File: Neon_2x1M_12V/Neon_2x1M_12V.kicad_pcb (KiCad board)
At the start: 2 copper layers, 77.5 x 51.5 mm, 47 parts, among them J2 Barrel_Jack_MountingPin, J4 Barrel_Jack_MountingPin, J5 Barrel_Jack_MountingPin, J6 Conn_01x03_Pin, Q1 IRLML2502TRPBF, Q2 IRLML2502TRPBF, Q3 BSS138, Q4 BSS138, Q5 BSS138, SW1 SW_Push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

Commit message: added vias to 12v routes
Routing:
- net +12V: vias 6 -> 7
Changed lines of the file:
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@@
-	)
-	(segment
-		(start 171.9 52.1)
-		(end 171.9 55.8)
-		(width 1.27)
-		(layer "F.Cu")
-		(net 1)
 	)
 	(segment
@@
 	)
 	(segment
-		(start 183.3 59.9)
-		(end 183.3 67.5)
-		(width 1.27)
-		(layer "F.Cu")
-		(net 1)
-	)
-	(segment
-		(start 171.9 55.8)
-		(end 171.9 63.9575)
+		(start 171.9 55.8)
+		(end 179.2 55.8)
 		(width 1.27)
 		(layer "F.Cu")
@@
 	)
 	(segment
-		(start 171.9 55.8)
-		(end 179.2 55.8)
-		(width 1.27)
-		(layer "F.Cu")
-		(net 1)
-	)
-	(segment
 		(start 171.9 63.9575)
 		(end 172.7 64.7575)
@@
 	)
 	(segment
+		(start 171.9 52.1)
+		(end 172.7 51.3)
+		(width 1.27)
+		(layer "F.Cu")
+		(net 1)
+	)
+	(segment
+		(start 179.2 55.8)
+		(end 183.3 59.9)
+		(width 1.27)
+		(layer "F.Cu")
+		(net 1)
+	)
+	(segment
+		(start 171.9 55.8)
+		(end 171.9 52.1)
+		(width 1.27)
+		(layer "F.Cu")
+		(net 1)
+	)
+	(segment
 		(start 118.367677 61)
 		(end 118.4 61)
@@
 	)
 	(segment
-		(start 172.7 51.3)
-		(end 171.9 52.1)
-		(width 1.27)
-		(layer "F.Cu")
-		(net 1)
-	)
-	(segment
 		(start 124.2 52)
 		(end 124.2 55.825)
@@
 	)
 	(segment
+		(start 118.367677 62.867677)
+		(end 118.367677 61)
+		(width 1.27)
+		(layer "F.Cu")
+		(net 1)
+	)
+	(segment
+		(start 171.9 55.8)
+		(end 171.9 63.9575)
+		(width 1.27)
+		(layer "F.Cu")
+		(net 1)
+	)
+	(segment
+		(start 183.3 59.9)
+		(end 183.3 67.5)
+		(width 1.27)
+		(layer "F.Cu")
+		(net 1)
+	)
+	(segment
+		(start 122.8 67.3)
+		(end 123.7 67.3)
+		(width 1.27)
+		(layer "F.Cu")
+		(net 1)
+	)
+	(segment
+		(start 159 72.6)
+		(end 170.8 72.6)
+		(width 1.27)
+		(layer "F.Cu")
+		(net 1)
+	)
+	(segment
+		(start 123.342676 56.025)
+		(end 121.683838 57.683838)
+		(width 1.27)
+		(layer "F.Cu")
+		(net 1)
+	)
+	(segment
+		(start 124 56.025)
+		(end 123.342676 56.025)
+		(width 1.27)
+		(layer "F.Cu")
+		(net 1)
+	)
+	(segment
 		(start 183.3 67.5)
 		(end 178.2 72.6)
-		(width 1.27)
-		(layer "F.Cu")
-		(net 1)
-	)
-	(segment
-		(start 118.367677 62.867677)
-		(end 118.367677 61)
-		(width 1.27)
-		(layer "F.Cu")
-		(net 1)
-	)
-	(segment
-		(start 179.2 55.8)
-		(end 183.3 59.9)
-		(width 1.27)
-		(layer "F.Cu")
-		(net 1)
-	)
-	(segment
-		(start 122.8 67.3)
-		(end 123.7 67.3)
-		(width 1.27)
-		(layer "F.Cu")
-		(net 1)
-	)
-	(segment
-		(start 159 72.6)
-		(end 170.8 72.6)
-		(width 1.27)
-		(layer "F.Cu")
-		(net 1)
-	)
-	(segment
-		(start 123.342676 56.025)
-		(end 121.683838 57.683838)
-		(width 1.27)
-		(layer "F.Cu")
-		(net 1)
-	)
-	(segment
-		(start 124 56.025)
-		(end 123.342676 56.025)
 		(width 1.27)
 		(layer "F.Cu")
@@
 	)
 	(via
+		(at 171.9 55.8)
+		(size 1.5)
+		(drill 0.75)
+		(layers "F.Cu" "B.Cu")
+		(net 1)
+	)
+	(via
 		(at 159 72.6)
 		(size 1.5)
@@
 		(drill 0.75)
 		(layers "F.Cu" "B.Cu")
+		(net 1)
+	)
+	(segment
+		(start 121.683838 57.683838)
+		(end 121.667676 57.7)
+		(width 1.27)
+		(layer "B.Cu")
+		(net 1)
+	)
+	(segment
+		(start 118.367677 59.032323)
+		(end 119.716162 57.683838)
+		(width 1.27)
+		(layer "B.Cu")
+		(net 1)
+	)
+	(segment
+		(start 124.2 52)
+		(end 122.7 50.5)
+		(width 1.27)
+		(layer "B.Cu")
+		(net 1)
+	)
+	(segment
+		(start 122.7 50.5)
+		(end 122.7 49.2)
+		(width 1.27)
+		(layer "B.Cu")
+		(net 1)
+	)
+	(segment
+		(start 171.9 52.1)
+		(end 172.7 51.3)
+		(width 1.27)
+		(layer "B.Cu")
+		(net 1)
+	)
+	(segment
+		(start 121.683838 57.683838)
+		(end 124.2 55.167677)
+		(width 1.27)
+		(layer "B.Cu")
+		(net 1)
+	)
+	(segment
+		(start 118.367677 62.867677)
+		(end 118.367677 61)
+		(width 1.27)
+		(layer "B.Cu")
+		(net 1)
+	)
+	(segment
+		(start 170.8 72.6)
+		(end 172.7 70.7)
+		(width 1.27)
+		(layer "B.Cu")
+		(net 1)
+	)
+	(segment
+		(start 171.9 55.8)
+		(end 171.9 63.9575)
+		(width 1.27)
+		(layer "B.Cu")
+		(net 1)
+	)
+	(segment
+		(start 119.99 64.49)
+		(end 120.09 64.49)
+		(width 1.27)
+		(layer "B.Cu")
+		(net 1)
+	)
+	(segment
+		(start 119.99 64.49)
+		(end 118.367677 62.867677)
+		(width 1.27)
+		(layer "B.Cu")
+		(net 1)
+	)
+	(segment
+		(start 119.716162 57.683838)
+		(end 121.683838 57.683838)
+		(width 1.27)
+		(layer "B.Cu")
+		(net 1)
+	)
+	(segment
+		(start 124.2 55.167677)
+		(end 124.2 53.3)
+		(width 1.27)
+		(layer "B.Cu")
+		(net 1)
+	)
+	(segment
+		(start 172.7 70.7)
+		(end 172.7 64.7575)
+		(width 1.27)
+		(layer "B.Cu")
+		(net 1)
+	)
+	(segment
+		(start 124.2 53.3)
+		(end 124.2 52)
+		(width 1.27)
+		(layer "B.Cu")
 		(net 1)
 	)
@@
 	)
 	(segment
-		(start 121.683838 57.683838)
-		(end 121.667676 57.7)
-		(width 1.27)
-		(layer "B.Cu")
-		(net 1)
-	)
-	(segment
-		(start 118.367677 59.032323)
-		(end 119.716162 57.683838)
-		(width 1.27)
-		(layer "B.Cu")
-		(net 1)
-	)
-	(segment
-		(start 124.2 52)
-		(end 122.7 50.5)
-		(width 1.27)
-		(layer "B.Cu")
-		(net 1)
-	)
-	(segment
-		(start 122.7 50.5)
-		(end 122.7 49.2)
-		(width 1.27)
-		(layer "B.Cu")
-		(net 1)
-	)
-	(segment
-		(start 121.683838 57.683838)
-		(end 124.2 55.167677)
-		(width 1.27)
-		(layer "B.Cu")
-		(net 1)
-	)
-	(segment
-		(start 118.367677 62.867677)
-		(end 118.367677 61)
-		(width 1.27)
-		(layer "B.Cu")
-		(net 1)
-	)
-	(segment
-		(start 170.8 72.6)
-		(end 172.7 70.7)
-		(width 1.27)
-		(layer "B.Cu")
-		(net 1)
-	)
-	(segment
-		(start 119.99 64.49)
-		(end 120.09 64.49)
-		(width 1.27)
-		(layer "B.Cu")
-		(net 1)
-	)
-	(segment
-		(start 119.99 64.49)
-		(end 118.367677 62.867677)
-		(width 1.27)
-		(layer "B.Cu")
-		(net 1)
-	)
-	(segment
-		(start 119.716162 57.683838)
-		(end 121.683838 57.683838)
-		(width 1.27)
-		(layer "B.Cu")
-		(net 1)
-	)
-	(segment
-		(start 124.2 55.167677)
-		(end 124.2 53.3)
-		(width 1.27)
-		(layer "B.Cu")
-		(net 1)
-	)
-	(segment
-		(start 172.7 70.7)
-		(end 172.7 64.7575)
-		(width 1.27)
-		(layer "B.Cu")
-		(net 1)
-	)
-	(segment
-		(start 124.2 53.3)
-		(end 124.2 52)
-		(width 1.27)
-		(layer "B.Cu")
-		(net 1)
-	)
-	(segment
 		(start 128.2 72.6)
 		(end 170.8 72.6)
@@
 	)
 	(segment
-		(start 171.9 52.1)
-		(end 172.7 51.3)
-		(width 1.27)
-		(layer "B.Cu")
-		(net 1)
-	)
-	(segment
 		(start 120.09 64.49)
 		(end 128.2 72.6)
@@
 	)
 	(segment
+		(start 171.9 55.8)
+		(end 171.9 52.1)
+		(width 1.27)
+		(layer "B.Cu")
+		(net 1)
+	)
+	(segment
 		(start 118.367677 61)
 		(end 118.367677 59.032323)
 		(width 1.27)
 		(layer "B.Cu")
-		(net 1)
-	)
-	(segment
-		(start 171.9 63.9575)
-		(end 171.9 52.1)
-		(width 1.27)
-		(layer "B.Cu")

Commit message: generated BOM
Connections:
- J2 pad 3: (no net) -> unconnected-(J2-MountPin-Pad3)
- J4 pad 3: (no net) -> unconnected-(J4-MountPin-Pad3)
- J5 pad 3: (no net) -> unconnected-(J5-MountPin-Pad3)
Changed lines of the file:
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@@
 	(net 54 "unconnected-(U1-SDI{slash}SD1-Pad22)")
 	(net 55 "unconnected-(U1-SCK{slash}CLK-Pad20)")
+	(net 56 "unconnected-(J2-MountPin-Pad3)")
+	(net 57 "unconnected-(J4-MountPin-Pad3)")
+	(net 58 "unconnected-(J5-MountPin-Pad3)")
 	(footprint "Resistor_SMD:R_0805_2012Metric_Pad1.20x1.40mm_HandSolder"
 		(layer "F.Cu")
@@
 			(remove_unused_layers no)
 			(roundrect_rratio 0.25)
+			(net 57 "unconnected-(J4-MountPin-Pad3)")
+			(pinfunction "MountPin")
+			(pintype "passive+no_connect")
 		)
 		(embedded_fonts no)
@@
 			(remove_unused_layers no)
 			(roundrect_rratio 0.25)
+			(net 58 "unconnected-(J5-MountPin-Pad3)")
+			(pinfunction "MountPin")
+			(pintype "passive+no_connect")
 		)
 		(embedded_fonts no)
@@
 			(remove_unused_layers no)
 			(roundrect_rratio 0.25)
+			(net 56 "unconnected-(J2-MountPin-Pad3)")
+			(pinfunction "MountPin")
+			(pintype "passive+no_connect")
 		)
 		(embedded_fonts no)

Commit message: generated production files
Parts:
- D5: value Blue LED -> Red Indicator LED
- Q3, Q4, Q5: value BSS138 -> Si2302DS
- R1: value 2.2k Ohm -> 820 Ohm
- R13: value 660 Ohm -> 680 Ohm
- R4: value 1k Ohm -> 820 Ohm
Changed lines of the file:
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@@
 			(outputformat 1)
 			(mirror no)
-			(drillshape 1)
+			(drillshape 0)
 			(scaleselection 1)
-			(outputdirectory "")
+			(outputdirectory "Production_Files/Gerbers/")
 		)
 	)
@@
 			)
 		)
-		(property "Value" "BSS138"
+		(property "Value" "Si2302DS"
 			(at 0 2.4 90)
 			(layer "F.Fab")
@@
 			)
 		)
-		(property "Datasheet" "https://www.onsemi.com/pub/Collateral/BSS138-D.PDF"
+		(property "Datasheet" "https://www.vishay.com/docs/68645/si2302cds.pdf"
 			(at 0 0 90)
 			(layer "F.Fab")
@@
 			)
 		)
-		(property "Description" "50V Vds, 0.22A Id, N-Channel MOSFET, SOT-23"
+		(property "Description" ""
 			(at 0 0 90)
 			(layer "F.Fab")
@@
 			)
 		)
-		(property "link" "https://makerselectronics.com/product/smd-mosfet-transistor-bss138-j1-50v-220ma-3-5%CF%8910v220ma-360mw-n-channel-sot-23/?srsltid=AfmBOorKPkIxsAwv-3Onwyym6kfiJ7AE8Pv9g0Pld8GAUTAgILHxbmr_"
+		(property "link" "https://uge-one.com/product/si2302ds-sot23-general-purpose-n-channel-mosfet-smd-transistor-sot-23/"
 			(at 0 0 90)
 			(unlocked yes)
@@
 			)
 		)
-		(property "Value" "2.2k Ohm"
+		(property "Value" "820 Ohm"
 			(at 0 1.83 90)
 			(layer "F.Fab")
@@
 			)
 		)
-		(property "Datasheet" "https://makerselectronics.com/product/chip-resistor-smd-2-2k%cf%89-%c2%b15-0-125w-%c2%b1100ppm-c-0805/"
+		(property "Datasheet" "https://uge-one.com/product/smd-chip-resistor-size-1206-820r-ohm/"
 			(at 0 0 90)
 			(layer "F.Fab")
@@
 			)
 		)
-		(property "link" "https://makerselectronics.com/product/chip-resistor-smd-2-2k%cf%89-%c2%b15-250mw-1206/"
+		(property "link" "https://uge-one.com/product/smd-chip-resistor-size-1206-820r-ohm/"
 			(at 0 0 270)
 			(unlocked yes)
@@
 			)
 		)
-		(property "Value" "Blue LED"
+		(property "Value" "Red Indicator LED"
 			(at 0 1.83 90)
 			(layer "F.Fab")
@@
 			)
 		)
-		(property "Value" "BSS138"
+		(property "Value" "Si2302DS"
 			(at 0.762922 2.733803 0)
 			(layer "F.Fab")
@@
 			)
 		)
-		(property "Datasheet" "https://www.onsemi.com/pub/Collateral/BSS138-D.PDF"
+		(property "Datasheet" "https://www.vishay.com/docs/68645/si2302cds.pdf"
 			(at 0 0 0)
 			(layer "F.Fab")
@@
 			)
 		)
-		(property "Description" "50V Vds, 0.22A Id, N-Channel MOSFET, SOT-23"
+		(property "Description" ""
 			(at 0 0 0)
 			(layer "F.Fab")
@@
 			)
 		)
-		(property "link" "https://makerselectronics.com/product/smd-mosfet-transistor-bss138-j1-50v-220ma-3-5%CF%8910v220ma-360mw-n-channel-sot-23/?srsltid=AfmBOorKPkIxsAwv-3Onwyym6kfiJ7AE8Pv9g0Pld8GAUTAgILHxbmr_"
+		(property "link" "https://uge-one.com/product/si2302ds-sot23-general-purpose-n-channel-mosfet-smd-transistor-sot-23/"
 			(at 0 0 0)
 			(unlocked yes)
@@
 			)
 		)
-		(property "Value" "BSS138"
+		(property "Value" "Si2302DS"
 			(at 0 2.4 90)
 			(layer "F.Fab")
@@
 			)
 		)
-		(property "Datasheet" "https://www.onsemi.com/pub/Collateral/BSS138-D.PDF"
+		(property "Datasheet" "https://www.vishay.com/docs/68645/si2302cds.pdf"
 			(at 0 0 90)
 			(layer "F.Fab")
@@
 			)
 		)
-		(property "Description" "50V Vds, 0.22A Id, N-Channel MOSFET, SOT-23"
+		(property "Description" ""
 			(at 0 0 90)
 			(layer "F.Fab")
@@
 			)
 		)
-		(property "link" "https://makerselectronics.com/product/smd-mosfet-transistor-bss138-j1-50v-220ma-3-5%CF%8910v220ma-360mw-n-channel-sot-23/?srsltid=AfmBOorKPkIxsAwv-3Onwyym6kfiJ7AE8Pv9g0Pld8GAUTAgILHxbmr_"
+		(property "link" "https://uge-one.com/product/si2302ds-sot23-general-purpose-n-channel-mosfet-smd-transistor-sot-23/"
 			(at 0 0 90)
 			(unlocked yes)
@@
 			)
 		)
-		(property "Value" "1k Ohm"
+		(property "Value" "820 Ohm"
 			(at 0 1.83 90)
 			(layer "F.Fab")
@@
 			)
 		)
-		(property "Datasheet" "https://makerselectronics.com/product/chip-resistor-smd-1k%cf%89-%c2%b15-0-125w-%c2%b1100ppm-%e2%84%83-0603/"
+		(property "Datasheet" "https://uge-one.com/product/smd-chip-resistor-size-1206-820r-ohm/"
 			(at 0 0 90)
 			(layer "F.Fab")
@@
 			)
 		)
-		(property "link" "https://makerselectronics.com/product/chip-resistor-smd-1k%cf%89-%c2%b15-0-25w-%c2%b1100ppm-%e2%84%83-1206-chip/"
+		(property "link" "https://uge-one.com/product/smd-chip-resistor-size-1206-820r-ohm/"
 			(at 0 0 90)
 			(unlocked yes)
@@
 			)
 		)
-		(property "Value" "660 Ohm"
+		(property "Value" "680 Ohm"
 			(at 0 1.83 90)
 			(layer "F.Fab")
@@
 		)
 		(embedded_fonts no)
-		(model "${KIPRJMOD}/Library/TS-1088-AR02016/TS-1088-AR02016.step"
+		(model "${KIPRJMOD}/Library/TS_button_3_4_2/TS_button_3_4_2.step"
 			(offset
 				(xyz 0 0 0)
@@
 		)
 		(embedded_fonts no)
-		(model "${KIPRJMOD}/Library/TS-1088-AR02016/TS-1088-AR02016.step"
+		(model "${KIPRJMOD}/Library/TS_button_3_4_2/TS_button_3_4_2.step"
 			(offset
 				(xyz 0 0 0)

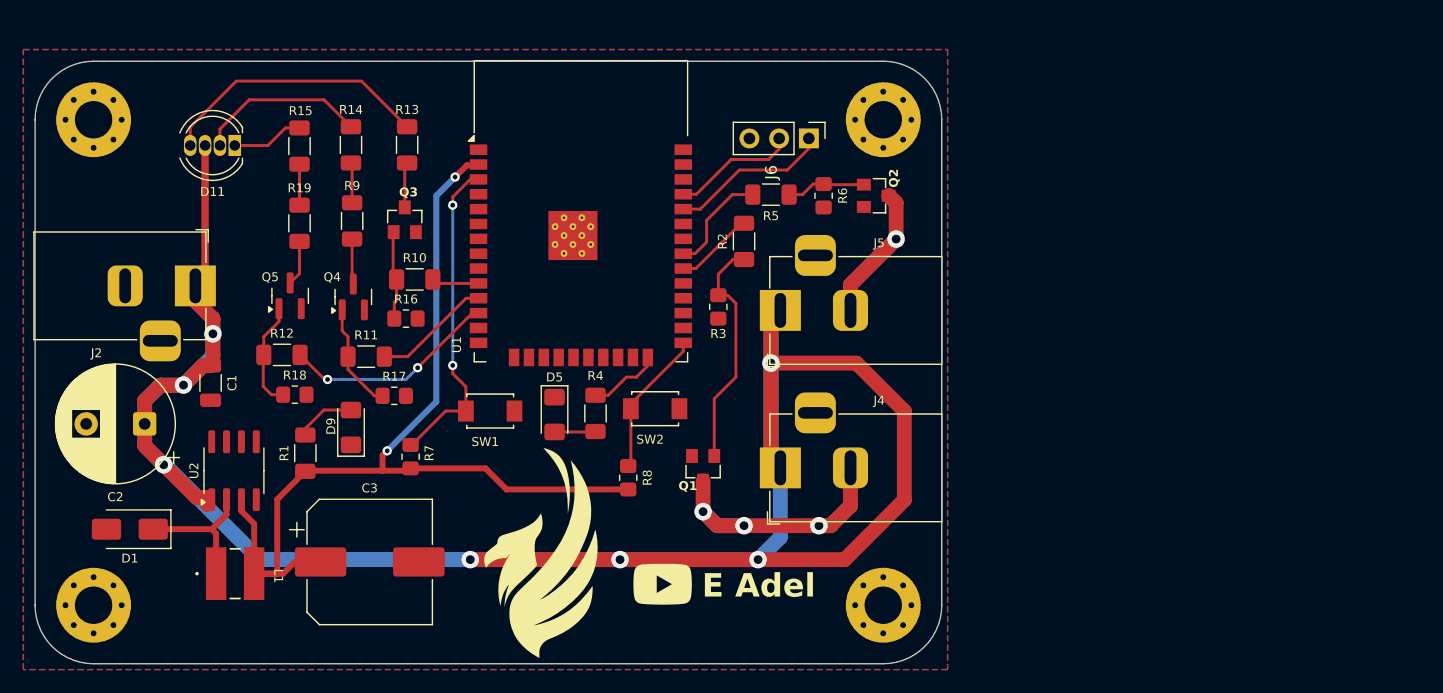
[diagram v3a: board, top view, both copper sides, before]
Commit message: initial commit remove old chinese buck converter and replace it with LM2596 DC DC converter adjustable
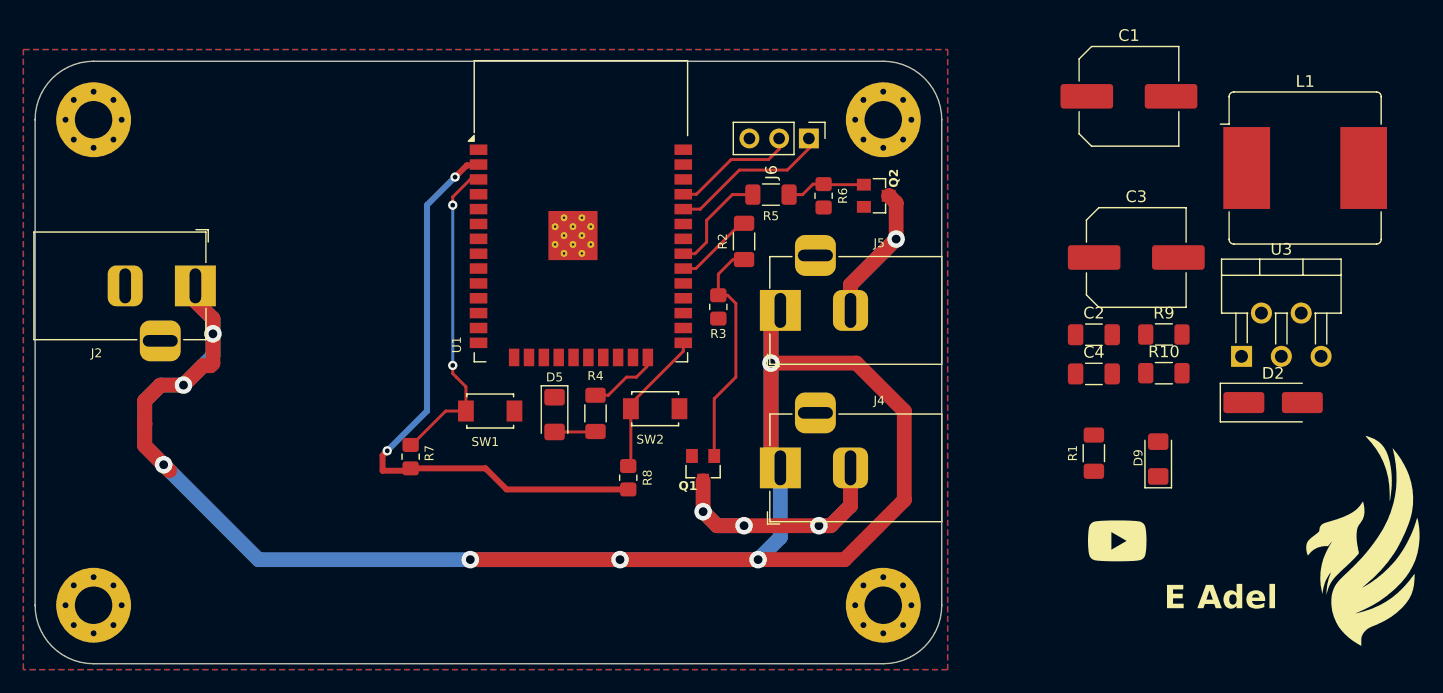
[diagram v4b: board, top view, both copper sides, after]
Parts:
- removed D1: 1N5822, Diode_SMD:D_SMA
- removed D11: LED_BGAR, LED_THT:LED_D5.0mm-4_RGB
- removed Q3: Si2302DS, custom_SOT23:custom_SOT23
- removed Q4, Q5: Si2302DS, Package_TO_SOT_SMD:SOT-23
- removed R11, R12: 220 Ohm, Resistor_SMD:R_1206_3216Metric_Pad1.30x1.75mm_HandSolder
- removed R13: 680 Ohm, Resistor_SMD:R_1206_3216Metric_Pad1.30x1.75mm_HandSolder
- removed R14, R15, R19: 300 Ohm, Resistor_SMD:R_1206_3216Metric_Pad1.30x1.75mm_HandSolder
- removed R16, R17, R18: 10k Ohm, Resistor_SMD:R_0805_2012Metric_Pad1.20x1.40mm_HandSolder
- removed U2: XL1509-3.3, Package_SO:SOIC-8_3.9x4.9mm_P1.27mm
- added C4: 100nF, Capacitor_SMD:C_1206_3216Metric_Pad1.33x1.80mm_HandSolder, F.Cu at (199.5, 56.7)
- added D2: SS34, Diode_SMD:D_SMA_Handsoldering, F.Cu at (214.8, 59.2)
- added U3: LM2596T-ADJ, Package_TO_SOT_THT:TO-220-5_P3.4x3.7mm_StaggerOdd_Lead3.8mm_Vertical, F.Cu at (212.1, 55.2)
- C1: value 1 uF -> 100uF; footprint Capacitor_SMD:C_1206_3216Metric -> Capacitor_SMD:C_Elec_8x10.2
- C2: value 470uF 35V -> 100nF; footprint Capacitor_THT:CP_Radial_D10.0mm_P5.00mm -> Capacitor_SMD:C_1206_3216Metric_Pad1.33x1.80mm_HandSolder
- C3: value 330uF 50V -> 220uF; footprint Capacitor_SMD:CP_Elec_10x10.5 -> Capacitor_SMD:C_Elec_8x10.2
- L1: value 47uH / 2A -> 47uH; footprint CD43_Inductor:CD43 -> Inductor_SMD:L_Bourns_SRR1208_12.7x12.7mm
- R10: value 220 Ohm -> 27K
- R9: value 300 Ohm -> 1.3K
- moved L1 97.8 mm to (217.6, 39.1)
- moved G*** 93.4 mm to (241.0, 54.5)
- moved C1 82.2 mm to (202.5, 33.0), turned to 0 degrees
- moved C2 81.5 mm to (199.5, 53.4), turned to 0 degrees
- moved C3 70.5 mm to (203.1, 46.8)
- moved G*** 70.3 mm to (223.3, 71.0)
- moved R9 70.1 mm to (205.5, 53.4), turned to 0 degrees
- moved D9 69.1 mm to (205.0, 64.0)
- moved R1 67.4 mm to (199.5, 63.5)
- moved R10 64.5 mm to (205.5, 56.7)
- moved G*** 39.0 mm to (201.5, 71.0)
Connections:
- R10 pad 1: Net-(Q3-G) -> +3V3
- R10 pad 2: ESP_IO25 -> Net-(U3-FB)
- R9 pad 1: Net-(R14-Pad2) -> Net-(U3-FB)
- R9 pad 2: Net-(Q4-D) -> GND
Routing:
- net +3V3: track 83.1 -> 51.9 mm
- net Net-(D11-RK): track 23.3 -> 0.00 mm
- net ESP_IO27: track 18.5 -> 0.00 mm, vias 2 -> 0
- net +12V: track 209.5 -> 192.4 mm
- net Net-(D11-GK): track 14.6 -> 0.00 mm
- net Net-(D2-K): track 12.0 -> 0.00 mm
- net ESP_IO26: track 10.1 -> 0.00 mm
- net Net-(Q5-G): track 9.20 -> 0.00 mm
- net Net-(Q4-G): track 9.19 -> 0.00 mm
- net Net-(Q3-G): track 7.66 -> 0.00 mm
- net Net-(D11-BK): track 6.15 -> 0.00 mm
- net Net-(D9-A): track 5.11 -> 0.00 mm
- net ESP_IO25: track 4.05 -> 0.00 mm
- net Net-(Q4-D): track 3.89 -> 0.00 mm
- net Net-(Q5-D): track 3.88 -> 0.00 mm
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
